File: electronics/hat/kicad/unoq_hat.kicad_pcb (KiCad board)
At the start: 4 copper layers, 68.6 x 53.3 mm, 87 parts, among them J1 JMEDIA 2x30 1.27 SMD male (GP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, J10 SM02B-SRSS-TB left foot conta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, J11 SM02B-SRSS-TB right foot cont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, J12 BM04B-SRSS-TB trunk IMU I2C, J2 JMISC 2x30 1.27 SMD male (GPE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, J3 TF31-22S-0.5SH 22p 0.5 FFC (I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, J4 BM06B-SRSS-TB ToF, J5 S3B-PH-SM4-TB servo bus, J6 S4B-PH-SM4-TB 2S pack in, J7 S2B-PH-SM4-TB speaker, J8 SM02B-SRSS-TB electret mic, J9 SM02B-SRSS-TB touch pad, Q1 MMBT3906, Q2 AON6407 reverse-polarity P-FET, U1 TCA9406DCUR, U2 TCA9555PWR, U3 TPS62933DRLR, U4 PAM8302AASCR, U5 SN74LVC1G126DBVR, U6 SN74LVC1G125DBVR, U7 LSM6DSV16X, U8 INA226AIDGSR, U9 TTP233H-BA6

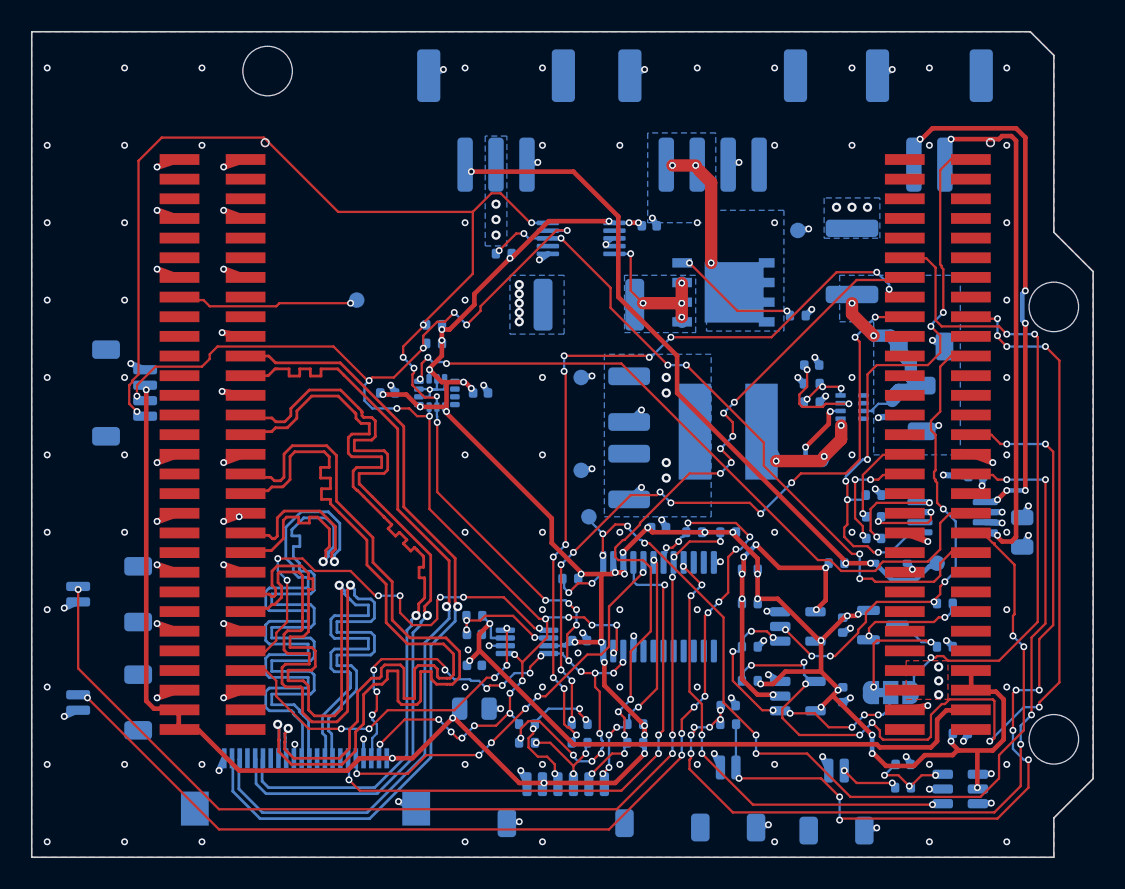
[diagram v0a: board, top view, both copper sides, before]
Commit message: hat rev C: boost to UNO Q VIN, EN divider fix, checks and docs
Rev C of the UNO Q head hat (foreman/microduck-assembly.60, 2026-10-10):
- TPS61088 boost (U10) makes 11.86 V from the 2S pack into the UNO Q VIN
  (JMEDIA 57/59); the hat no longer back-feeds the UNO Q 5 V.
- U10 EN now sits on a 100k/100k divider from VBAT_B. Earlier Rev C builds
  tied EN to VCC, the output of an LDO that EN itself enables, so the boost
  would never have started. DRC and ERC could not see it.
- Interrupts on 3.3 V MCU pins, D40 isolates the servo pull-ups.
- kicad_dru no longer carries a 0.09 mm clearance rule: it replaced the
  0.127 mm zone clearance and filled GND inside the JMEDIA mask openings.

Checks: kicad-cli DRC 0 errors / 0 warnings / 0 unconnected (board rules and
JLC rules), ERC 0/0, schematic vs board 75/75 nets. Docs: footprint table
(51 parts), strap pins (29 rows), power budget, BOM with live stock.

Co-Authored-By: Claude Opus 5.5 <noreply@anthropic.com>
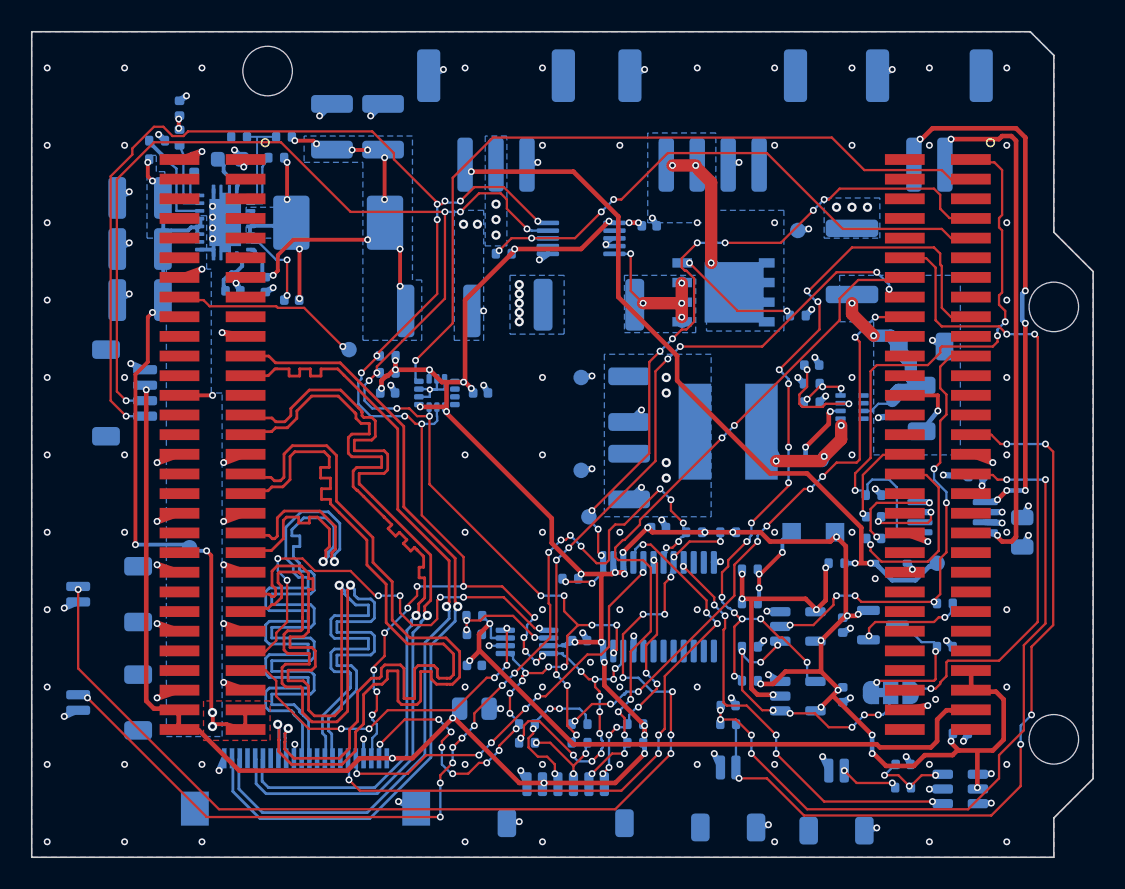
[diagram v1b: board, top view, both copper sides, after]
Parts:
- added C30: 22uF 25V, C_1210_3225Metric, B.Cu at (19.4, 6.14)
- added C31: 22uF 25V, C_1210_3225Metric, B.Cu at (22.7, 6.14)
- added C32: 100nF 25V, C_0402_1005Metric, B.Cu at (15.1, 16.3)
- added C33: 4.7uF 16V, C_0603_1608Metric, B.Cu at (12.8, 8.24)
- added C34: 100nF 25V, C_0402_1005Metric, B.Cu at (16.8, 17.3)
- added C35: 47nF, C_0402_1005Metric, B.Cu at (13.0, 16.7)
- added C36: 6.8nF, C_0402_1005Metric, B.Cu at (9.55, 4.94)
- added C37: 22uF 25V, C_1210_3225Metric, B.Cu at (7.00, 10.7)
- added C38: 22uF 25V, C_1210_3225Metric, B.Cu at (7.00, 14.0)
- added C39: 22uF 25V, C_1210_3225Metric, B.Cu at (7.00, 17.3)
- added D40: BAT54H,115, BAT54H_Nexperia_SOD123F, B.Cu at (50.5, 32.3)
- added F2: JK-MSMD500L-12V 5A PTC, Fuse_1812_4532Metric, B.Cu at (26.3, 18.0)
- added L2: FXL0630-2R2-M 2.2uH, L_Changjiang_FXL0630, B.Cu at (19.8, 12.3)
- added R30: 300k, R_0402_1005Metric, B.Cu at (15.8, 8.14)
- added R31: 150k, R_0402_1005Metric, B.Cu at (10.5, 8.54)
- added R32: 1M, R_0402_1005Metric, B.Cu at (8.10, 8.24)
- added R33: 113k, R_0402_1005Metric, B.Cu at (8.10, 7.04)
- added R34: 18k, R_0402_1005Metric, B.Cu at (9.55, 6.84)
- added R35: 100k, R_0402_1005Metric, B.Cu at (16.3, 6.79)
- added R36: 100k, R_0402_1005Metric, B.Cu at (13.4, 6.79)
- added TP7: VIN12, TestPoint_Pad_D1.0mm, B.Cu at (10.2, 33.3)
- added U10: TPS61088RHLR, Texas_VQFN-RHL-20, B.Cu at (12.5, 12.3)
- C1, C10, C13, C14, C15, C19, C2, C20, C21, C22, C23, C24, C25, C26, C3, C5, C8, C9: footprint Capacitor_SMD:C_0402_1005Metric -> C_0402_1005Metric
- C11, C12: footprint Capacitor_SMD:C_1210_3225Metric -> C_1210_3225Metric
- C16, C4: footprint Capacitor_SMD:C_0805_2012Metric -> C_0805_2012Metric
- C6, C7: footprint Capacitor_SMD:C_1206_3216Metric -> C_1206_3216Metric
- D1: footprint Diode_SMD:D_SOD-323 -> D_SOD-323
- F1: footprint Fuse:Fuse_1812_4532Metric -> Fuse_1812_4532Metric
- H2, H3, H4: footprint MountingHole:MountingHole_3.2mm_M3 -> MountingHole_3.2mm_M3
- J1, J2: footprint unoq_hat:UNOQ_JMEDIA_2x30_P1.27_Male -> UNOQ_JMEDIA_2x30_P1.27_Male
- J10, J11, J8, J9: footprint Connector_JST:JST_SH_SM02B-SRSS-TB_1x02-1MP_P1.00mm_Horizontal -> JST_SH_SM02B-SRSS-TB_1x02-1MP_P1.00mm_Horizontal
- J12: footprint Connector_JST:JST_SH_BM04B-SRSS-TB_1x04-1MP_P1.00mm_Vertical -> JST_SH_BM04B-SRSS-TB_1x04-1MP_P1.00mm_Vertical
- J3: footprint unoq_hat:FFC_22P_P0.5_TF31-22S -> FFC_22P_P0.5_TF31-22S
- J4: footprint Connector_JST:JST_SH_BM06B-SRSS-TB_1x06-1MP_P1.00mm_Vertical -> JST_SH_BM06B-SRSS-TB_1x06-1MP_P1.00mm_Vertical
- J5: footprint Connector_JST:JST_PH_S3B-PH-SM4-TB_1x03-1MP_P2.00mm_Horizontal -> JST_PH_S3B-PH-SM4-TB_1x03-1MP_P2.00mm_Horizontal
- J6: footprint Connector_JST:JST_PH_S4B-PH-SM4-TB_1x04-1MP_P2.00mm_Horizontal -> JST_PH_S4B-PH-SM4-TB_1x04-1MP_P2.00mm_Horizontal
- J7: footprint Connector_JST:JST_PH_S2B-PH-SM4-TB_1x02-1MP_P2.00mm_Horizontal -> JST_PH_S2B-PH-SM4-TB_1x02-1MP_P2.00mm_Horizontal
- JP1: footprint Jumper:SolderJumper-3_P1.3mm_Bridged12_RoundedPad1.0x1.5mm -> SolderJumper-3_P1.3mm_Bridged12_RoundedPad1.0x1.5mm
- L1: footprint unoq_hat:FNR6045_6.0x6.0mm -> FNR6045_6.0x6.0mm
- Q1: footprint Package_TO_SOT_SMD:SOT-23 -> SOT-23
- Q2: footprint Package_SO:PowerPAK_SO-8_Single -> PowerPAK_SO-8_Single
- R1, R11, R12, R13, R14, R15, R16, R17, R18, R19, R2, R20, R21, R24, R25, R26, R27, R28, R29, R3, R4, R5, R6, R7, R8, R9: footprint Resistor_SMD:R_0402_1005Metric -> R_0402_1005Metric
- R22: footprint Resistor_SMD:R_2512_6332Metric -> R_2512_6332Metric
- TP1, TP2, TP3, TP4, TP5, TP6: footprint TestPoint:TestPoint_Pad_D1.0mm -> TestPoint_Pad_D1.0mm
- U1: footprint Package_SO:VSSOP-8_2.3x2mm_P0.5mm -> VSSOP-8_2.3x2mm_P0.5mm
- U2: footprint Package_SO:TSSOP-24_4.4x7.8mm_P0.65mm -> TSSOP-24_4.4x7.8mm_P0.65mm
- U3: footprint Package_TO_SOT_SMD:SOT-583-8 -> SOT-583-8
- U4: footprint Package_SO:MSOP-8_3x3mm_P0.65mm -> MSOP-8_3x3mm_P0.65mm
- U5, U6: footprint Package_TO_SOT_SMD:SOT-23-5 -> SOT-23-5
- U7: footprint Package_LGA:LGA-14_3x2.5mm_P0.5mm_LayoutBorder3x4y -> LGA-14_3x2.5mm_P0.5mm_LayoutBorder3x4y
- U8: footprint Package_SO:TSSOP-10_3x3mm_P0.5mm -> TSSOP-10_3x3mm_P0.5mm
- U9: footprint Package_TO_SOT_SMD:SOT-23-6 -> SOT-23-6
- moved R28 3.61 mm to (23.0, 20.9)
- moved R27 3.55 mm to (23.0, 22.0)
- moved TP1 3.24 mm to (20.5, 20.5)
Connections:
- J1 pad 10: unconnected-(J1-Pin_10-Pad10) -> (no net)
- J1 pad 11: unconnected-(J1-Pin_11-Pad11) -> (no net)
- J1 pad 12: unconnected-(J1-Pin_12-Pad12) -> (no net)
- J1 pad 15: unconnected-(J1-Pin_15-Pad15) -> (no net)
- J1 pad 17: unconnected-(J1-Pin_17-Pad17) -> (no net)
- J1 pad 18: unconnected-(J1-Pin_18-Pad18) -> (no net)
- J1 pad 22: unconnected-(J1-Pin_22-Pad22) -> (no net)
- J1 pad 24: unconnected-(J1-Pin_24-Pad24) -> (no net)
- J1 pad 28: unconnected-(J1-Pin_28-Pad28) -> (no net)
- J1 pad 3: unconnected-(J1-Pin_3-Pad3) -> (no net)
- J1 pad 30: unconnected-(J1-Pin_30-Pad30) -> (no net)
- J1 pad 34: unconnected-(J1-Pin_34-Pad34) -> (no net)
- J1 pad 36: unconnected-(J1-Pin_36-Pad36) -> (no net)
- J1 pad 4: unconnected-(J1-Pin_4-Pad4) -> (no net)
- J1 pad 40: unconnected-(J1-Pin_40-Pad40) -> (no net)
- J1 pad 42: unconnected-(J1-Pin_42-Pad42) -> (no net)
- J1 pad 46: unconnected-(J1-Pin_46-Pad46) -> (no net)
- J1 pad 48: unconnected-(J1-Pin_48-Pad48) -> (no net)
- J1 pad 5: unconnected-(J1-Pin_5-Pad5) -> (no net)
- J1 pad 52: unconnected-(J1-Pin_52-Pad52) -> (no net)
- J1 pad 54: unconnected-(J1-Pin_54-Pad54) -> (no net)
- J1 pad 57: unconnected-(J1-Pin_57-Pad57) -> VIN12
- J1 pad 59: unconnected-(J1-Pin_59-Pad59) -> VIN12
- J1 pad 6: unconnected-(J1-Pin_6-Pad6) -> (no net)
- J1 pad 9: unconnected-(J1-Pin_9-Pad9) -> (no net)
- J2 pad 10: unconnected-(J2-Pin_10-Pad10) -> (no net)
- J2 pad 11: unconnected-(J2-Pin_11-Pad11) -> (no net)
- J2 pad 13: unconnected-(J2-Pin_13-Pad13) -> (no net)
- J2 pad 15: unconnected-(J2-Pin_15-Pad15) -> (no net)
- J2 pad 19: unconnected-(J2-Pin_19-Pad19) -> (no net)
- J2 pad 2: unconnected-(J2-Pin_2-Pad2) -> (no net)
- J2 pad 20: unconnected-(J2-Pin_20-Pad20) -> (no net)
- J2 pad 22: unconnected-(J2-Pin_22-Pad22) -> (no net)
- J2 pad 23: unconnected-(J2-Pin_23-Pad23) -> (no net)
- J2 pad 24: unconnected-(J2-Pin_24-Pad24) -> (no net)
- J2 pad 25: unconnected-(J2-Pin_25-Pad25) -> (no net)
- J2 pad 28: unconnected-(J2-Pin_28-Pad28) -> (no net)
- J2 pad 3: unconnected-(J2-Pin_3-Pad3) -> IMU_INT1
- J2 pad 30: unconnected-(J2-Pin_30-Pad30) -> (no net)
- J2 pad 36: unconnected-(J2-Pin_36-Pad36) -> (no net)
- J2 pad 37: IMU_INT1 -> (no net)
- J2 pad 38: unconnected-(J2-Pin_38-Pad38) -> (no net)
- J2 pad 39: EXP_INT -> (no net)
- J2 pad 4: unconnected-(J2-Pin_4-Pad4) -> (no net)
- J2 pad 41: INA_ALERT -> (no net)
- J2 pad 42: unconnected-(J2-Pin_42-Pad42) -> (no net)
- J2 pad 43: unconnected-(J2-Pin_43-Pad43) -> (no net)
- J2 pad 45: unconnected-(J2-Pin_45-Pad45) -> (no net)
- J2 pad 46: unconnected-(J2-Pin_46-Pad46) -> (no net)
- J2 pad 47: unconnected-(J2-Pin_47-Pad47) -> (no net)
- J2 pad 48: unconnected-(J2-Pin_48-Pad48) -> (no net)
- J2 pad 49: unconnected-(J2-Pin_49-Pad49) -> (no net)
- J2 pad 5: unconnected-(J2-Pin_5-Pad5) -> (no net)
- J2 pad 50: unconnected-(J2-Pin_50-Pad50) -> (no net)
- J2 pad 51: unconnected-(J2-Pin_51-Pad51) -> (no net)
- J2 pad 52: unconnected-(J2-Pin_52-Pad52) -> (no net)
- J2 pad 54: V5 -> (no net)
- J2 pad 56: V5 -> (no net)
- J2 pad 59: unconnected-(J2-Pin_59-Pad59) -> (no net)
- J2 pad 6: unconnected-(J2-Pin_6-Pad6) -> (no net)
- J2 pad 60: unconnected-(J2-Pin_60-Pad60) -> (no net)
- J2 pad 7: unconnected-(J2-Pin_7-Pad7) -> EXP_INT
- J2 pad 8: unconnected-(J2-Pin_8-Pad8) -> (no net)
- J2 pad 9: unconnected-(J2-Pin_9-Pad9) -> INA_ALERT
- R15 pad 2: +3V3 -> SERVO_PULLUP
- R21 pad 2: +3V3 -> SERVO_PULLUP
- U2 pad 10: unconnected-(U2-P06-Pad10) -> (no net)
- U2 pad 11: unconnected-(U2-P07-Pad11) -> (no net)
- U2 pad 13: unconnected-(U2-P10-Pad13) -> (no net)
- U2 pad 14: unconnected-(U2-P11-Pad14) -> (no net)
- U2 pad 15: unconnected-(U2-P12-Pad15) -> (no net)
- U2 pad 16: unconnected-(U2-P13-Pad16) -> (no net)
- U2 pad 17: unconnected-(U2-P14-Pad17) -> (no net)
- U2 pad 18: unconnected-(U2-P15-Pad18) -> (no net)
- U2 pad 19: unconnected-(U2-P16-Pad19) -> (no net)
- U2 pad 20: unconnected-(U2-P17-Pad20) -> (no net)
- U3 pad 1: unconnected-(U3-RT-Pad1) -> (no net)
- U3 pad 2: unconnected-(U3-EN-Pad2) -> (no net)
- U4 pad 2: unconnected-(U4-NC-Pad2) -> (no net)
- U7 pad 10: unconnected-(U7-OCS_Aux-Pad10) -> (no net)
- U7 pad 11: unconnected-(U7-SDO_Aux-Pad11) -> (no net)
- U7 pad 9: unconnected-(U7-INT2-Pad9) -> (no net)
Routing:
- net VIN12: track 0.00 -> 49.6 mm, vias 0 -> 7
- net CCI_SDA: track 88.1 -> 117.8 mm, vias 22 -> 27
- net VBAT_B: track 0.00 -> 28.9 mm, vias 0 -> 10
- net EXP_INT: track 63.7 -> 48.8 mm, vias 10 -> 11
- net SW2: track 0.00 -> 14.0 mm, vias 0 -> 4
- net SERVO_RX: track 64.4 -> 52.6 mm, vias 11 -> 14
- net GND: track 80.2 -> 89.6 mm, vias 156 -> 162
- net INA_ALERT: track 44.4 -> 36.6 mm, vias 7 -> 4
- net BST_FB: track 0.00 -> 6.85 mm
- net MCU_SDA: track 45.6 -> 39.0 mm, vias 11 -> 9
- net BST_EN: track 0.00 -> 6.08 mm
- net MIC_BIAS: track 54.5 -> 48.5 mm, vias 10 -> 6
- net SERVO_PULLUP: track 0.00 -> 5.79 mm, vias 0 -> 3
- net BST_BOOT: track 0.00 -> 5.46 mm, vias 0 -> 2
- net CCI_SCL: track 124.4 -> 129.5 mm, vias 29 -> 33
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- added copper zone on B.Cu, net SW2
- added copper zone on B.Cu, net VBAT_B
- added copper zone on B.Cu, net VIN12
- added copper zone on F.Cu, net VIN12
- removed copper zone on F.Cu, net V5
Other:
- board text added: "C30"
- board text added: "C31"
- board text added: "C32"
- board text added: "C33"
- board text added: "C34"
- board text added: "C35"
- board text added: "C36"
- board text added: "C37"
- board text added: "C38"
- board text added: "C39"
- board text added: "D40"
- board text added: "F2"
- board text added: "L2"
- board text added: "R30"
- board text added: "R31"
- board text added: "R32"
- board text added: "R33"
- board text added: "R34"
- board text added: "R35"
- board text added: "R36"
- board text added: "TP7"
- board text added: "U10"

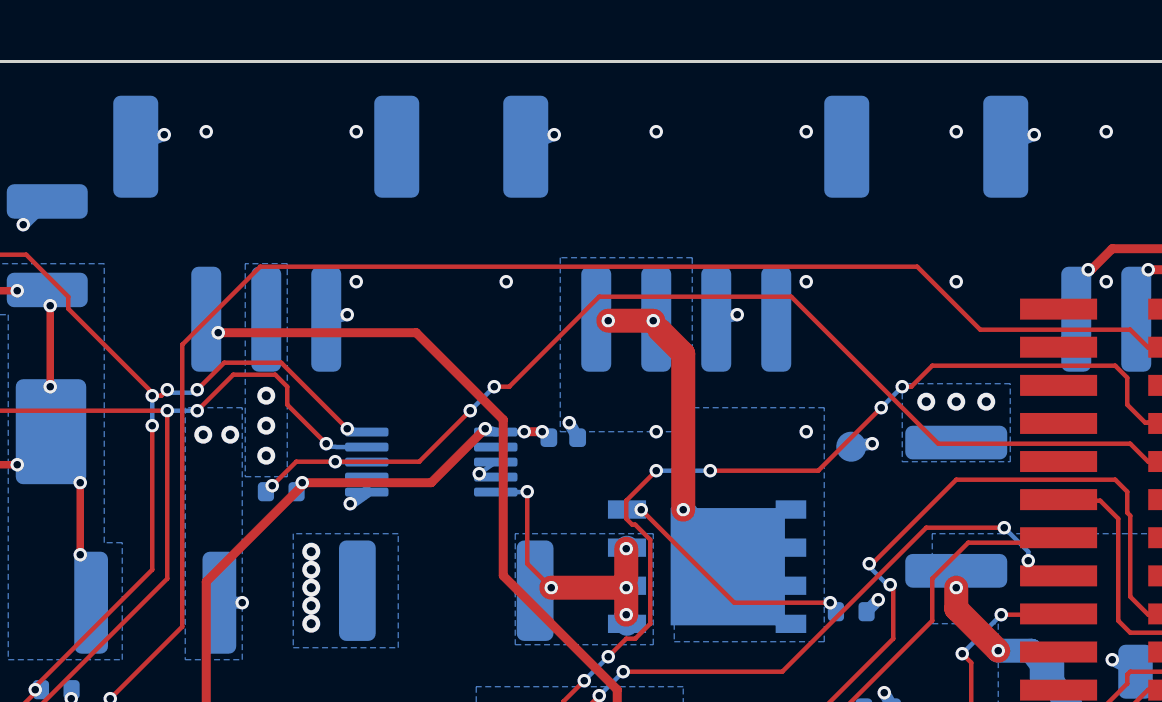
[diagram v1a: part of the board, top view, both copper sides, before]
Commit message: hat Rev C build #10: 6-pin J6 (6 A), order sheet for 2026-10-11
- J6 is now S6B-PH-SM4-TB (C265405), three contacts per pole: 6 A vs 4.72 A worst case
- VBAT_IN pour widened for J6; KiCad DRC 0/0/0 (board and JLC rules), ERC 0/0, 75/75 nets
- fab: gerbers.zip, bom.csv (55 lines), cpl.csv (95 parts); BOM in stock for 5 boards at 14:53Z
- ce-fabmcp pcb_drc on build #10: In1/In2 PASS, F/B approximation FAIL explained
- docs/PCB-ORDER-LEIF-2026-10-11.md: one-page order sheet with J6-to-XT30 pigtail kit line

Signed: foreman/microduck-assembly.60

Co-Authored-By: Claude Opus 5.5 <noreply@anthropic.com>
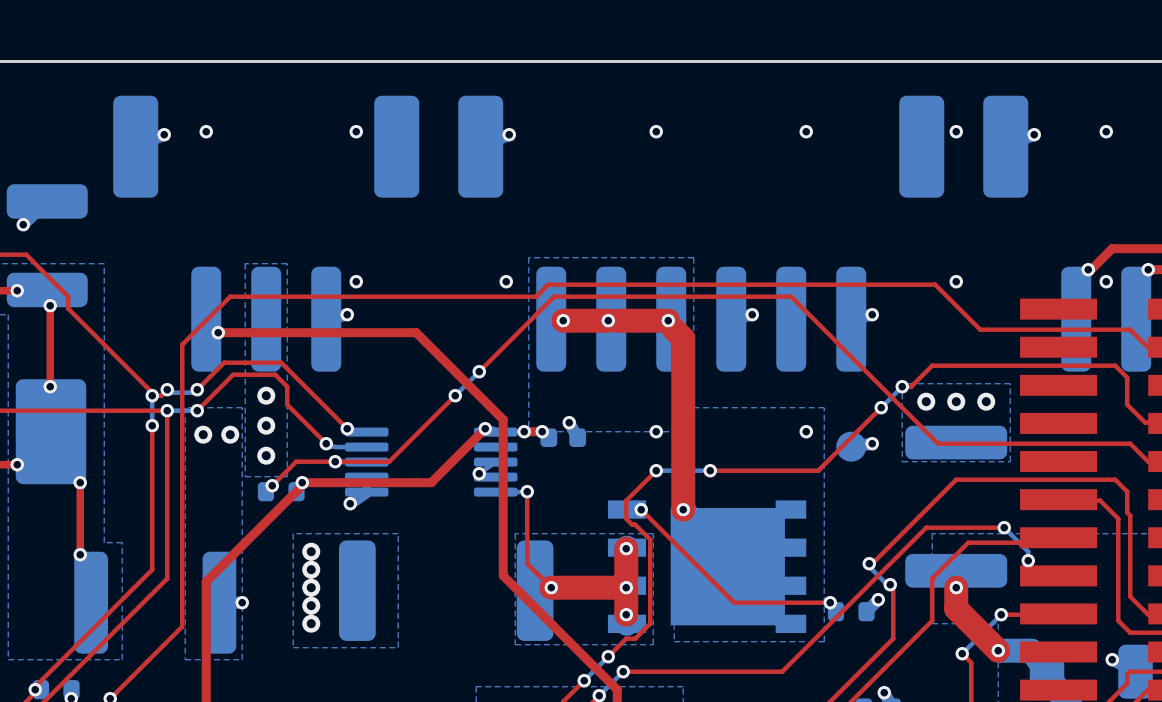
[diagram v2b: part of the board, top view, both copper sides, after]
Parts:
- J6: value S4B-PH-SM4-TB 2S pack in -> S6B-PH-SM4-TB 2S pack in; footprint JST_PH_S4B-PH-SM4-TB_1x04-1MP_P2.00mm_Horizontal -> JST_PH_S6B-PH-SM4-TB_1x06-1MP_P2.00mm_Horizontal
- moved J6 0.50 mm to (44.5, 5.74)
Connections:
- J6 pad 3: GND -> VBAT_IN
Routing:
- net VBAT_IN: track 10.8 -> 12.4 mm, vias 3 -> 4
- net GND: track 89.6 -> 90.4 mm
